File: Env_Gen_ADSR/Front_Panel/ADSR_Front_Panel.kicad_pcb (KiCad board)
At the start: 2 copper layers, 30 x 128.5 mm, 5 parts

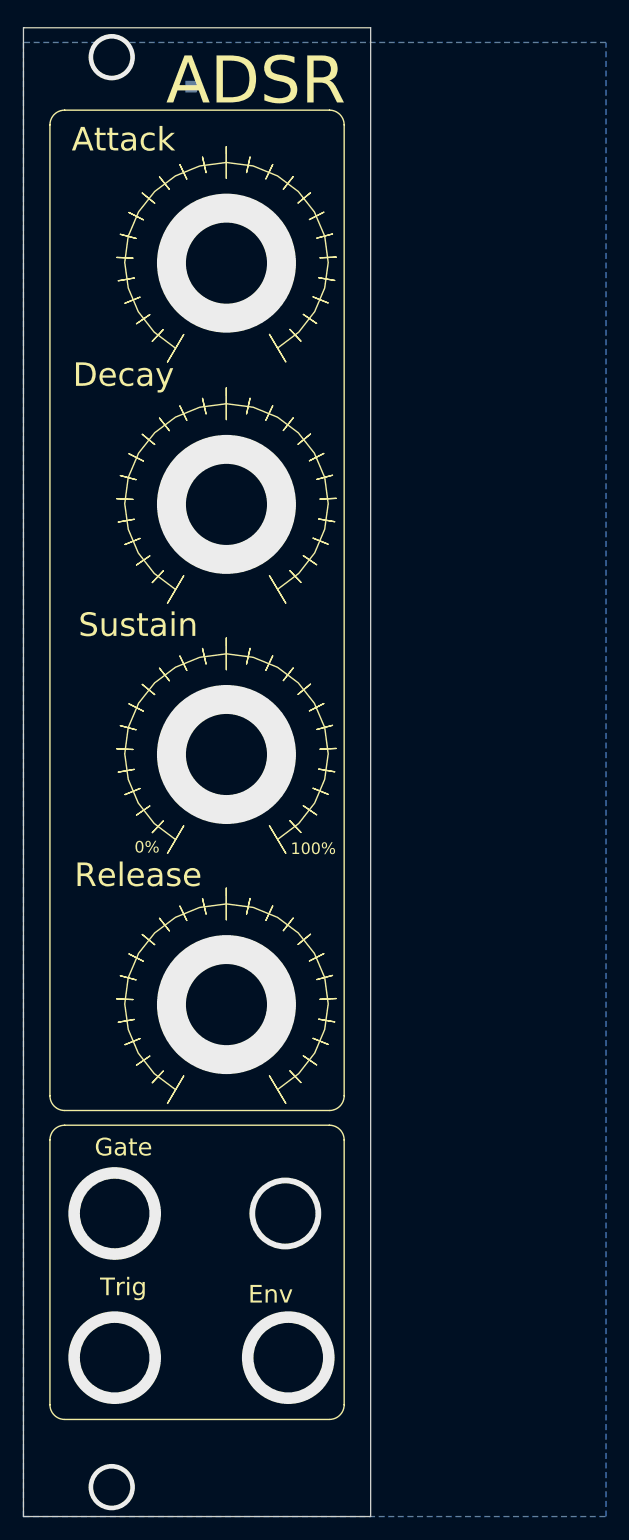
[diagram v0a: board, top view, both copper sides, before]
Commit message: Fix envelope generator front panel size and alignment with IO board.
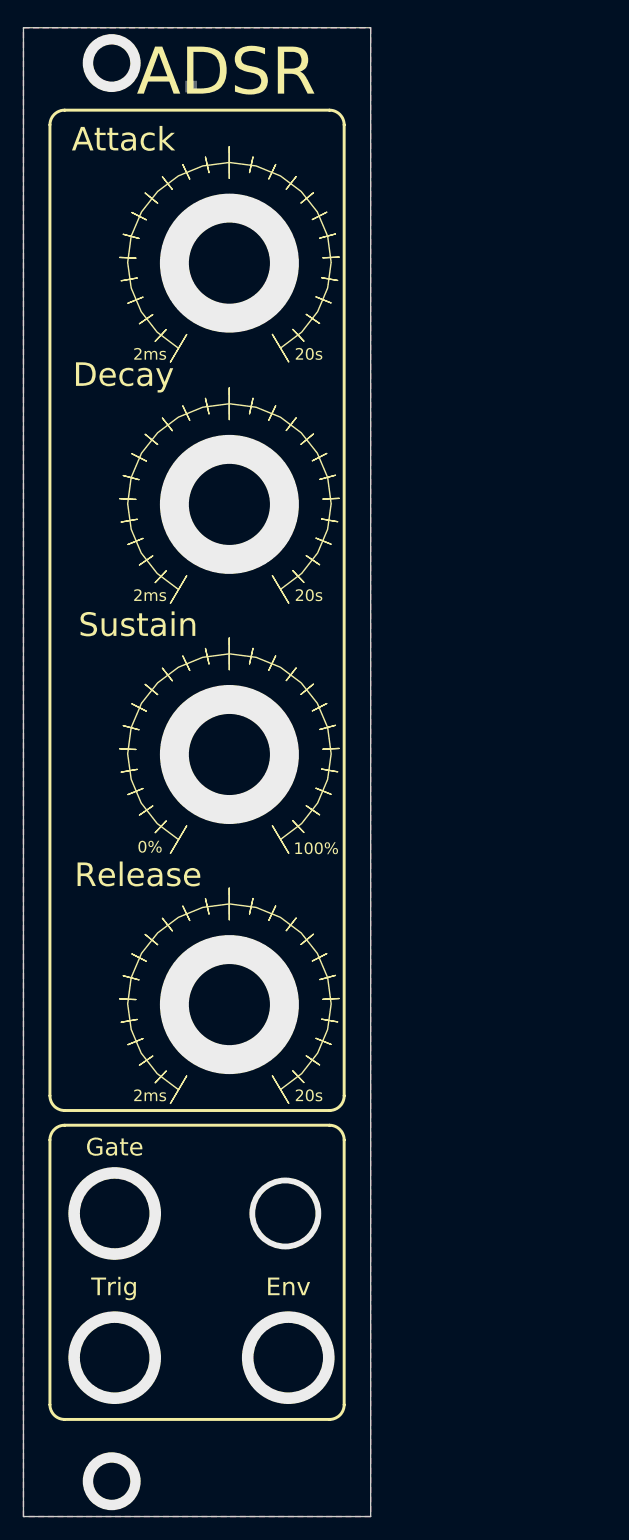
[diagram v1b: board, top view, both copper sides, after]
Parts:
- removed the tick_marks at (81.3, 123.4)
- removed the tick_marks at (81.3, 101.9)
- added tick_marks: G***, AS3340_VCO_FP:knob_tick_marks, F.Cu at (81.5, 123.4)
- added tick_marks: G***, AS3340_VCO_FP:knob_tick_marks, F.Cu at (81.5, 101.9)
- moved tick_marks 0.25 mm to (81.5, 80.3)
- moved tick_marks 0.25 mm to (81.5, 59.4)
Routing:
- added copper zone on F.Cu, net GND
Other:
- board text added: "20s"
- board text added: "2ms"
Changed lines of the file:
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@@
-(kicad_pcb (version 20171130) (host pcbnew "(5.1.2-1)-1")
+(kicad_pcb (version 20171130) (host pcbnew 5.1.4)
   (general
     (thickness 1.6)
-    (drawings 31)
+    (drawings 37)
     (tracks 10)
     (zones 0)
@@
   (layers
     (0 F.Cu signal)
-    (31 B.Cu signal hide)
+    (31 B.Cu signal)
     (32 B.Adhes user)
     (33 F.Adhes user)
@@
   )
   (module AS3340_VCO_FP:knob_tick_marks (layer F.Cu)
-    (at 81.28 123.444)
+    (at 81.534 123.444)
     (descr "Imported from knob_tick_marks.svg")
     (tags svg2mod)
@@
   )
   (module AS3340_VCO_FP:knob_tick_marks (layer F.Cu)
-    (at 81.28 101.854)
+    (at 81.534 101.854)
     (descr "Imported from knob_tick_marks.svg")
     (tags svg2mod)
@@
   )
   (module AS3340_VCO_FP:knob_tick_marks (layer F.Cu)
-    (at 81.28 80.264)
+    (at 81.534 80.264)
     (descr "Imported from knob_tick_marks.svg")
     (tags svg2mod)
@@
   )
   (module AS3340_VCO_FP:knob_tick_marks (layer F.Cu)
-    (at 81.28 59.436)
+    (at 81.534 59.436)
     (descr "Imported from knob_tick_marks.svg")
     (tags svg2mod)
@@
       (net 1 GND))
   )
-  (gr_line (start 67.31 160.02) (end 90.17 160.02) (layer F.SilkS) (width 0.12))
-  (gr_arc (start 67.31 158.75) (end 66.04 158.75) (angle -90) (layer F.SilkS) (width 0.12))
-  (gr_line (start 66.04 135.89) (end 66.04 158.75) (layer F.SilkS) (width 0.12))
-  (gr_arc (start 90.17 158.75) (end 90.17 160.02) (angle -90) (layer F.SilkS) (width 0.12))
-  (gr_line (start 91.44 158.75) (end 91.44 135.89) (layer F.SilkS) (width 0.12))
-  (gr_text Env (at 85.09 149.225) (layer F.SilkS)
-    (effects (font (size 1.524 1.524) (thickness 0.2032)))
-  )
-  (gr_text Trig (at 72.39 148.59) (layer F.SilkS)
-    (effects (font (size 1.524 1.524) (thickness 0.2032)))
-  )
-  (gr_text Gate (at 72.39 136.525) (layer F.SilkS)
-    (effects (font (size 1.524 1.524) (thickness 0.2032)))
-  )
-  (gr_text 100% (at 88.773 110.744) (layer F.SilkS)
-    (effects (font (size 1 1) (thickness 0.15)))
-  )
-  (gr_text 0% (at 74.422 110.617) (layer F.SilkS)
-    (effects (font (size 1 1) (thickness 0.15)))
-  )
-  (gr_line (start 67.31 133.35) (end 90.17 133.35) (layer F.SilkS) (width 0.12))
-  (gr_arc (start 67.31 132.08) (end 66.04 132.08) (angle -90) (layer F.SilkS) (width 0.12))
-  (gr_arc (start 90.17 132.08) (end 90.17 133.35) (angle -90) (layer F.SilkS) (width 0.12))
+  (gr_text 20s (at 88.392 68.072) (layer F.SilkS)
+    (effects (font (size 1 1) (thickness 0.15)))
+  )
+  (gr_text 20s (at 88.392 88.9) (layer F.SilkS)
+    (effects (font (size 1 1) (thickness 0.15)))
+  )
+  (gr_text 2ms (at 74.676 88.9) (layer F.SilkS)
+    (effects (font (size 1 1) (thickness 0.15)))
+  )
+  (gr_text 2ms (at 74.676 68.072) (layer F.SilkS)
+    (effects (font (size 1 1) (thickness 0.15)))
+  )
+  (gr_text 20s (at 88.392 132.08) (layer F.SilkS)
+    (effects (font (size 1 1) (thickness 0.15)))
+  )
+  (gr_text 2ms (at 74.676 132.08) (layer F.SilkS)
+    (effects (font (size 1 1) (thickness 0.15)))
+  )
+  (gr_line (start 67.31 160.02) (end 90.17 160.02) (layer F.SilkS) (width 0.254))
+  (gr_arc (start 67.31 158.75) (end 66.04 158.75) (angle -90) (layer F.SilkS) (width 0.254))
+  (gr_line (start 66.04 135.89) (end 66.04 158.75) (layer F.SilkS) (width 0.254))
+  (gr_arc (start 90.17 158.75) (end 90.17 160.02) (angle -90) (layer F.SilkS) (width 0.254))
+  (gr_line (start 91.44 158.75) (end 91.44 135.89) (layer F.SilkS) (width 0.254))
+  (gr_text Env (at 86.614 148.59) (layer F.SilkS)
+    (effects (font (size 1.524 1.524) (thickness 0.254)))
+  )
+  (gr_text Trig (at 71.628 148.59) (layer F.SilkS)
+    (effects (font (size 1.524 1.524) (thickness 0.254)))
+  )
+  (gr_text Gate (at 71.628 136.525) (layer F.SilkS)
+    (effects (font (size 1.524 1.524) (thickness 0.254)))
+  )
+  (gr_text 100% (at 89.027 110.744) (layer F.SilkS)
+    (effects (font (size 1 1) (thickness 0.15)))
+  )
+  (gr_text 0% (at 74.676 110.617) (layer F.SilkS)
+    (effects (font (size 1 1) (thickness 0.15)))
+  )
+  (gr_line (start 67.31 133.35) (end 90.17 133.35) (layer F.SilkS) (width 0.254))
+  (gr_arc (start 67.31 132.08) (end 66.04 132.08) (angle -90) (layer F.SilkS) (width 0.254))
+  (gr_arc (start 90.17 132.08) (end 90.17 133.35) (angle -90) (layer F.SilkS) (width 0.254))
   (gr_text Release (at 73.66 113.03) (layer F.SilkS)
-    (effects (font (size 2.032 2.032) (thickness 0.2032)))
+    (effects (font (size 2.032 2.032) (thickness 0.254)))
   )
   (gr_text Sustain (at 73.66 91.44) (layer F.SilkS)
-    (effects (font (size 2.032 2.032) (thickness 0.2032)))
+    (effects (font (size 2.032 2.032) (thickness 0.254)))
   )
   (gr_text "ADSR Front Panel Rev 1" (at 92.202 56.134 90) (layer B.SilkS)
     (effects (font (size 1.5 1.5) (thickness 0.3)) (justify mirror))
   )
-  (gr_line (start 91.44 48.26) (end 91.44 132.08) (layer F.SilkS) (width 0.12))
-  (gr_line (start 66.04 132.08) (end 66.04 48.26) (layer F.SilkS) (width 0.12))
-  (gr_line (start 67.31 46.99) (end 90.17 46.99) (layer F.SilkS) (width 0.12))
-  (gr_arc (start 90.17 48.26) (end 91.44 48.26) (angle -90) (layer F.SilkS) (width 0.12))
-  (gr_arc (start 67.31 48.26) (end 67.31 46.99) (angle -90) (layer F.SilkS) (width 0.12))
+  (gr_line (start 91.44 48.26) (end 91.44 132.08) (layer F.SilkS) (width 0.254))
+  (gr_line (start 66.04 132.08) (end 66.04 48.26) (layer F.SilkS) (width 0.254))
+  (gr_line (start 67.31 46.99) (end 90.17 46.99) (layer F.SilkS) (width 0.254))
+  (gr_arc (start 90.17 48.26) (end 91.44 48.26) (angle -90) (layer F.SilkS) (width 0.254))
+  (gr_arc (start 67.31 48.26) (end 67.31 46.99) (angle -90) (layer F.SilkS) (width 0.254))
   (gr_text Attack (at 72.39 49.53) (layer F.SilkS)
-    (effects (font (size 2.032 2.032) (thickness 0.2032)))
-  )
-  (gr_text "ADSR\n" (at 83.82 44.45) (layer F.SilkS)
+    (effects (font (size 2.032 2.032) (thickness 0.254)))
+  )
+  (gr_text "ADSR\n" (at 81.28 43.688) (layer F.SilkS)
     (effects (font (size 4.064 4.064) (thickness 0.4064)))
   )
   (gr_text Decay (at 72.39 69.85) (layer F.SilkS)
-    (effects (font (size 2.032 2.032) (thickness 0.2032)))
-  )
-  (gr_arc (start 67.31 135.89) (end 67.31 134.62) (angle -90) (layer F.SilkS) (width 0.12))
-  (gr_line (start 90.17 134.62) (end 67.31 134.62) (layer F.SilkS) (width 0.12))
-  (gr_arc (start 90.17 135.89) (end 91.44 135.89) (angle -90) (layer F.SilkS) (width 0.12))
+    (effects (font (size 2.032 2.032) (thickness 0.254)))
+  )
+  (gr_arc (start 67.31 135.89) (end 67.31 134.62) (angle -90) (layer F.SilkS) (width 0.254))
+  (gr_line (start 90.17 134.62) (end 67.31 134.62) (layer F.SilkS) (width 0.254))
+  (gr_arc (start 90.17 135.89) (end 91.44 135.89) (angle -90) (layer F.SilkS) (width 0.254))
   (gr_line (start 63.754 168.402) (end 63.754 39.878) (layer Edge.Cuts) (width 0.05))
   (gr_line (start 93.726 168.402) (end 63.754 168.402) (layer Edge.Cuts) (width 0.05))
@@
   (gr_line (start 63.754 39.878) (end 93.726 39.878) (layer Edge.Cuts) (width 0.05))
   (via (at 86.36 142.24) (size 6.2) (drill 5.2) (layers F.Cu B.Cu) (net 1))
-  (via (at 81.28 102.616) (size 11.999999) (drill 7.000001) (layers F.Cu B.Cu) (net 1))
-  (via (at 81.28 124.206) (size 11.999999) (drill 7.000001) (layers F.Cu B.Cu) (net 1))
+  (via (at 81.534 102.616) (size 11.999999) (drill 7.000001) (layers F.Cu B.Cu) (net 1))
+  (via (at 81.534 124.206) (size 11.999999) (drill 7.000001) (layers F.Cu B.Cu) (net 1))
   (via (at 86.614 154.686) (size 7.999999) (drill 6.000001) (layers F.Cu B.Cu) (net 1))
   (via (at 71.628 142.24) (size 7.999999) (drill 6.000001) (layers F.Cu B.Cu) (net 1))
   (via (at 71.628 154.686) (size 7.999999) (drill 6.000001) (layers F.Cu B.Cu) (net 1))
-  (via (at 81.28 81.026) (size 11.999999) (drill 7.000001) (layers F.Cu B.Cu) (net 1))
-  (via (at 81.28 60.198) (size 11.999999) (drill 7.000001) (layers F.Cu B.Cu) (net 1))
-  (via (at 71.374 42.418) (size 4) (drill 3.2004) (layers F.Cu B.Cu) (net 1))
-  (via (at 71.374 165.862) (size 4) (drill 3.2004) (layers F.Cu B.Cu) (net 1))
-  (zone (net 1) (net_name GND) (layer B.Cu) (hatch edge 0.508)
-    (connect_pads yes (clearance 0.508))
+  (via (at 81.534 81.026) (size 11.999999) (drill 7.000001) (layers F.Cu B.Cu) (net 1))
+  (via (at 81.534 60.198) (size 11.999999) (drill 7.000001) (layers F.Cu B.Cu) (net 1))
+  (via (at 71.374 42.926) (size 4.99999) (drill 3.2004) (layers F.Cu B.Cu) (net 1))
+  (via (at 71.374 165.354) (size 4.99999) (drill 3.2004) (layers F.Cu B.Cu) (net 1))
+  (zone (net 1) (net_name GND) (layer F.Cu) (hatch edge 0.508)
+    (connect_pads (clearance 0.508))
     (min_thickness 0.254)
     (fill yes (arc_segments 32) (thermal_gap 0.508) (thermal_bridge_width 0.508))
     (polygon
       (pts
-        (xy 63.754 168.402) (xy 114.046 168.402) (xy 114.046 41.148) (xy 63.754 41.148)
+        (xy 63.754 39.878) (xy 93.726 39.878) (xy 93.726 168.402) (xy 63.754 168.402)
       )
     )
+  )
+  (zone (net 1) (net_name GND) (layer B.Cu) (hatch edge 0.508)
+    (connect_pads (clearance 0.508))
+    (min_thickness 0.254)
+    (fill yes (arc_segments 32) (thermal_gap 0.508) (thermal_bridge_width 0.508))
+    (polygon
+      (pts
+        (xy 63.754 39.878) (xy 93.726 39.878) (xy 93.726 168.402) (xy 63.754 168.402)
+      )
+    )

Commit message: Clean up envelope generator boards
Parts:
- added REF**: OSHW-Logo2_7.3x6mm_SilkScreen, Symbol:OSHW-Logo2_7.3x6mm_SilkScreen, B.Cu at (70.9, 52.1)
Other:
- board text added: "ADSR Env Gen Front Panel Rev 1"
- board text removed: "ADSR Front Panel Rev 1"

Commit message: Bunch of bug fixes and tweaks
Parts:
- removed TP1: TestPoint, TestPoint:TestPoint_Pad_1.0x1.0mm
- removed the tick_marks at (81.5, 123.4)
- removed the tick_marks at (81.5, 101.9)
- removed the tick_marks at (81.5, 80.3)
- removed the tick_marks at (81.5, 59.4)
- added H1: Attack, Eurorack:pot_fp_hole, F.Cu at (81.5, 60.2)
- added H2: Gate, Eurorack:pot_fp_hole, F.Cu at (81.5, 81.0)
- added H3: Decay, Eurorack:pot_fp_hole, F.Cu at (81.5, 102.6)
- added H4: Trigger, Eurorack:pot_fp_hole, F.Cu at (81.5, 124.2)
- added H5: Sustain, Eurorack:jack_fp_hole, F.Cu at (71.6, 142.2)
- added H6: Env, Eurorack:jack_fp_hole, F.Cu at (71.6, 154.7)
- added H7: Release, Eurorack:jack_fp_hole, F.Cu at (86.6, 154.7)
- added H8: TopMH, Eurorack:eurorack_mounting_hole, F.Cu at (71.4, 42.9)
- added H9: BottomMH, Eurorack:eurorack_mounting_hole, F.Cu at (71.4, 165.4)
- added tick_marks: G***, Eurorack:knob_tick_marks, F.Cu at (81.5, 123.4)
- added tick_marks: G***, Eurorack:knob_tick_marks, F.Cu at (81.5, 102.1)
- added tick_marks: G***, Eurorack:knob_tick_marks, F.Cu at (81.5, 80.5)
- added tick_marks: G***, Eurorack:knob_tick_marks, F.Cu at (81.5, 59.7)
- moved REF** 13.8 mm to (82.4, 44.5)
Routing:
- net GND: vias 10 -> 1

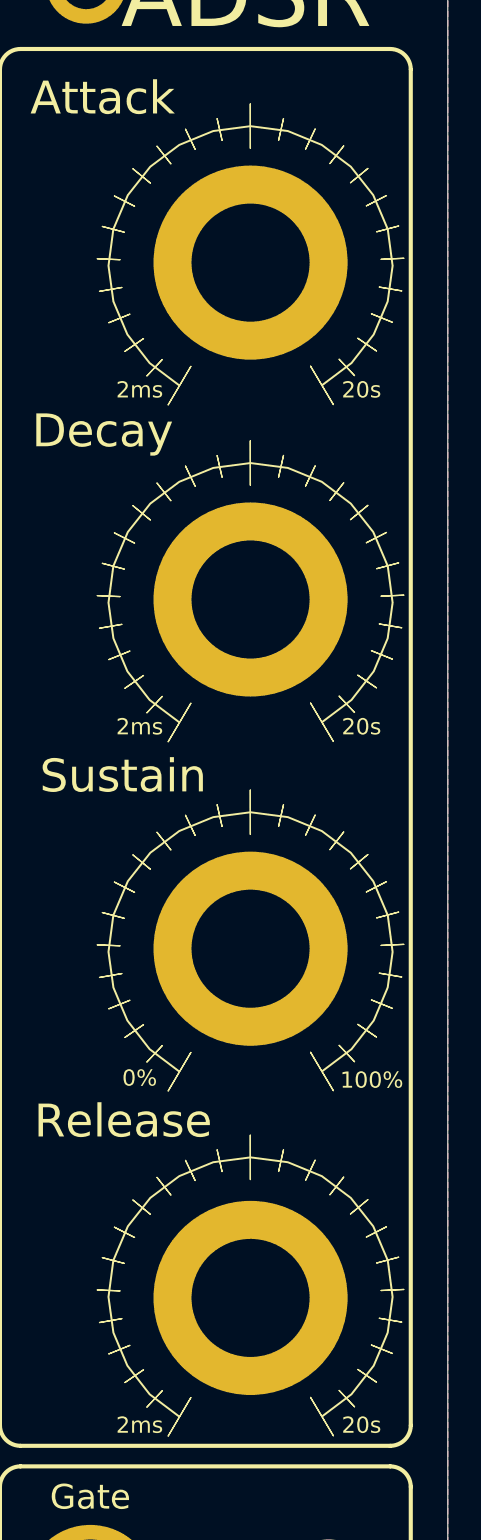
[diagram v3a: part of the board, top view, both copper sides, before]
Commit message: Clean up envelope gen board
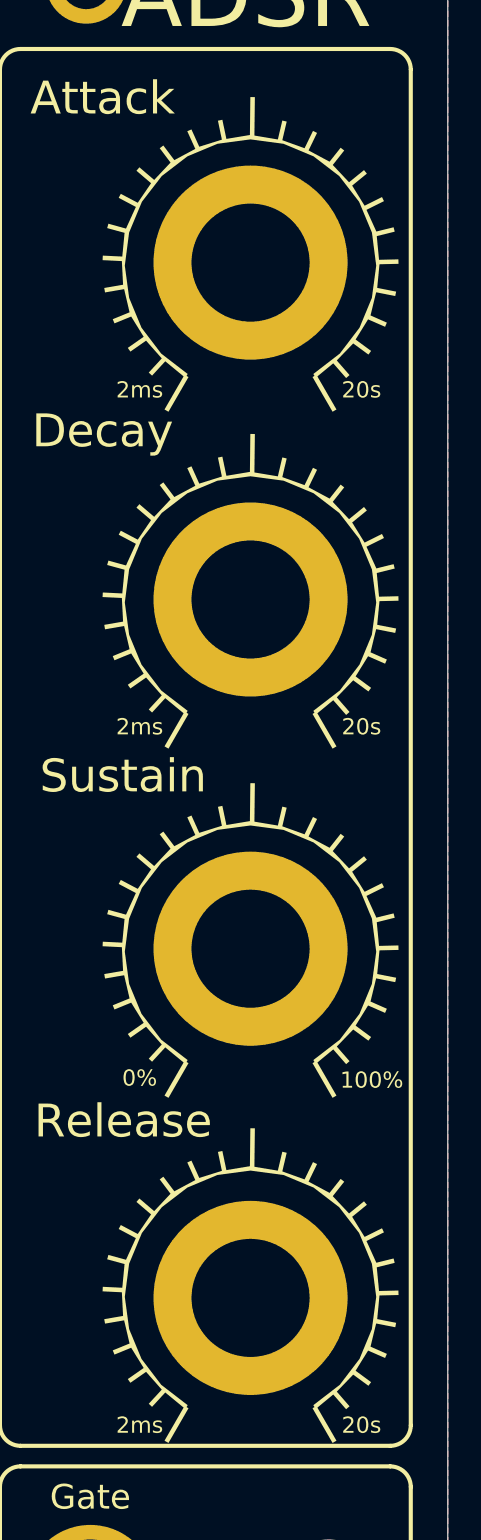
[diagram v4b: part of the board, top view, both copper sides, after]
